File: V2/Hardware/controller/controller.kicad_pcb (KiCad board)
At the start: 2 copper layers, 50 parts, among them J0 Molex_PSU_F, J2 Flat_7seg_F, J3 Rpi_DATA_F_3.3V, Q0 BD139-16, Q1 BD139-16, Q2 BD139-16, Q3 BD139-16, Q4 BD139-16, Q5 BD139-16, Q6 BD139-16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

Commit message: Update files
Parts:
- C5: value 1000uF 35V LOW ESR -> 100uF 25V LOW ESR; footprint Capacitor_THT:CP_Radial_D13.0mm_P5.00mm -> Capacitor_THT:CP_Radial_D6.3mm_P2.50mm
- moved C5 4.00 mm to (138.0, 107.0)
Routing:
- net Earth: track 514.3 -> 563.1 mm
- net /+12V: track 239.9 -> 251.5 mm
- net /5V+: track 77.5 -> 87.2 mm
- net Net-(Q0-Pad3): track 4.03 -> 5.15 mm

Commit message: update capacitors
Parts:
- C5: value 100uF 25V LOW ESR -> 1000uF 35V LOW ESR; footprint Capacitor_THT:CP_Radial_D6.3mm_P2.50mm -> Capacitor_THT:CP_Radial_D12.5mm_P5.00mm
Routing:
- net Earth: track 563.1 -> 558.4 mm

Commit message: Update controller
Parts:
- added C6: 1nF, Capacitor_THT:C_Disc_D5.0mm_W2.5mm_P5.00mm, F.Cu at (145.0, 43.0)
- added L0: 22uH, Inductor_THT:L_Axial_L7.0mm_D3.3mm_P10.16mm_Horizontal_Fastron_MICC, F.Cu at (125.0, 65.0)
- C1: value 47uF -> 10uF 16V LOW ESR; footprint Capacitor_THT:CP_Radial_D10.0mm_P5.00mm -> Capacitor_THT:CP_Radial_D5.0mm_P2.00mm
- moved C3 19.2 mm to (131.0, 43.0)
- moved C2 10.8 mm to (138.0, 43.0)
- moved R7 10.4 mm to (121.0, 63.0), turned to 180 degrees
- moved C1 3.16 mm to (129.0, 51.0)
- moved D1 2.00 mm to (115.5, 57.0)
- moved R8 1.00 mm to (135.0, 46.0), turned to 0 degrees
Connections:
- C1 pad 1: /5V+ -> Net-(C1-Pad1)
- C2 pad 1: /5V+ -> Net-(C1-Pad1)
- C3 pad 1: /5V+ -> Net-(C1-Pad1)
- R7 pad 1: /5V+ -> Net-(D1-Pad2)
- R7 pad 2: Net-(D1-Pad2) -> /5V+
- R8 pad 2: /5V+ -> Net-(C1-Pad1)
- U1 pad 20: /5V+ -> Net-(C1-Pad1)
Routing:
- net Net-(C1-Pad1): track 0.00 -> 70.6 mm
- net /5V+: track 87.2 -> 51.7 mm
- net Earth: track 558.4 -> 591.2 mm
- net Net-(R8-Pad1): track 7.83 -> 14.4 mm
- net Net-(D1-Pad2): track 12.4 -> 11.4 mm

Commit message: revision 2 boards
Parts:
- added Screw: MountingHole_3.2mm_M3, MountingHole:MountingHole_3.2mm_M3, F.Cu at (109.0, 106.0)
- added Screw: MountingHole_3.2mm_M3, MountingHole:MountingHole_3.2mm_M3, F.Cu at (192.0, 104.0)
- added Screw: MountingHole_3.2mm_M3, MountingHole:MountingHole_3.2mm_M3, F.Cu at (204.0, 41.0)
- added Screw: MountingHole_3.2mm_M3, MountingHole:MountingHole_3.2mm_M3, F.Cu at (108.0, 68.0)
- J0: value Molex_PSU_F -> Molex_PSU; footprint PSU:conn_hdd_15-24-4441 -> KicadLib:conn_hdd_15-24-4449
- J2: value Flat_7seg_F -> 7SEG_12V; footprint Connector_PinHeader_2.54mm:PinHeader_2x05_P2.54mm_Horizontal -> Connector_IDC:IDC-Header_2x05-1MP_P2.54mm_Latch_Vertical
- J3: value Rpi_DATA_F_3.3V -> RPI_DATA_3.3V; footprint Connector_PinHeader_2.54mm:PinHeader_2x03_P2.54mm_Horizontal -> Connector_IDC:IDC-Header_2x05-1MP_P2.54mm_Latch_Vertical
- moved L0 35.4 mm to (94.0, 48.0), turned to 270 degrees
- moved R7 22.6 mm to (99.0, 58.0), turned to 90 degrees
- moved J3 12.1 mm to (98.0, 87.0)
- moved J0 11.2 mm to (99.0, 43.0), turned to 180 degrees
- moved R12 10.0 mm to (127.0, 91.0), turned to 90 degrees
- moved D1 8.43 mm to (109.5, 51.0), turned to 270 degrees
- moved J2 7.27 mm to (173.0, 104.0), turned to 270 degrees
- moved R11 5.10 mm to (120.0, 91.0), turned to 90 degrees
- moved R10 4.84 mm to (113.0, 91.0)
- moved R9 4.47 mm to (106.0, 90.2)
- moved R13 3.01 mm to (123.0, 39.0)
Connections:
- J3 pad 1: /BIT_D -> /BIT_A
- J3 pad 2: Net-(J3-Pad2) -> Earth
- J3 pad 3: /BIT_C -> /BIT_B
- J3 pad 4: /BIT_C -> Earth
- J3 pad 5: /BIT_B -> /BIT_C
- J3 pad 6: /BIT_A -> Earth
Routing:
- net /SEG_C: track 17.8 -> 67.3 mm
- net /SEG_B: track 25.6 -> 71.2 mm
- net /SEG_A: track 36.9 -> 79.6 mm
- net /BIT_B: track 83.2 -> 41.9 mm, vias 2 -> 0
- net Net-(C1-Pad1): track 70.6 -> 105.2 mm
- net /5V+: track 51.7 -> 20.2 mm
- net /SEG_G: track 58.7 -> 37.8 mm
- net Net-(D5-Pad2): track 26.7 -> 8.00 mm
- net /SEG_F: track 47.1 -> 29.7 mm
- net /BIT_A: track 58.6 -> 44.0 mm
- net /SEG_E: track 34.3 -> 21.9 mm
- net Earth: track 591.2 -> 601.1 mm
- net /BIT_D: track 38.7 -> 45.1 mm
- net Net-(D6-Pad2): track 19.1 -> 25.1 mm
- net Net-(D3-Pad2): track 14.0 -> 8.00 mm
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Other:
- board text added: "125 mm"
- board text added: "83 mm"
- board text removed: "12.5cm"
- board text removed: "8cm"

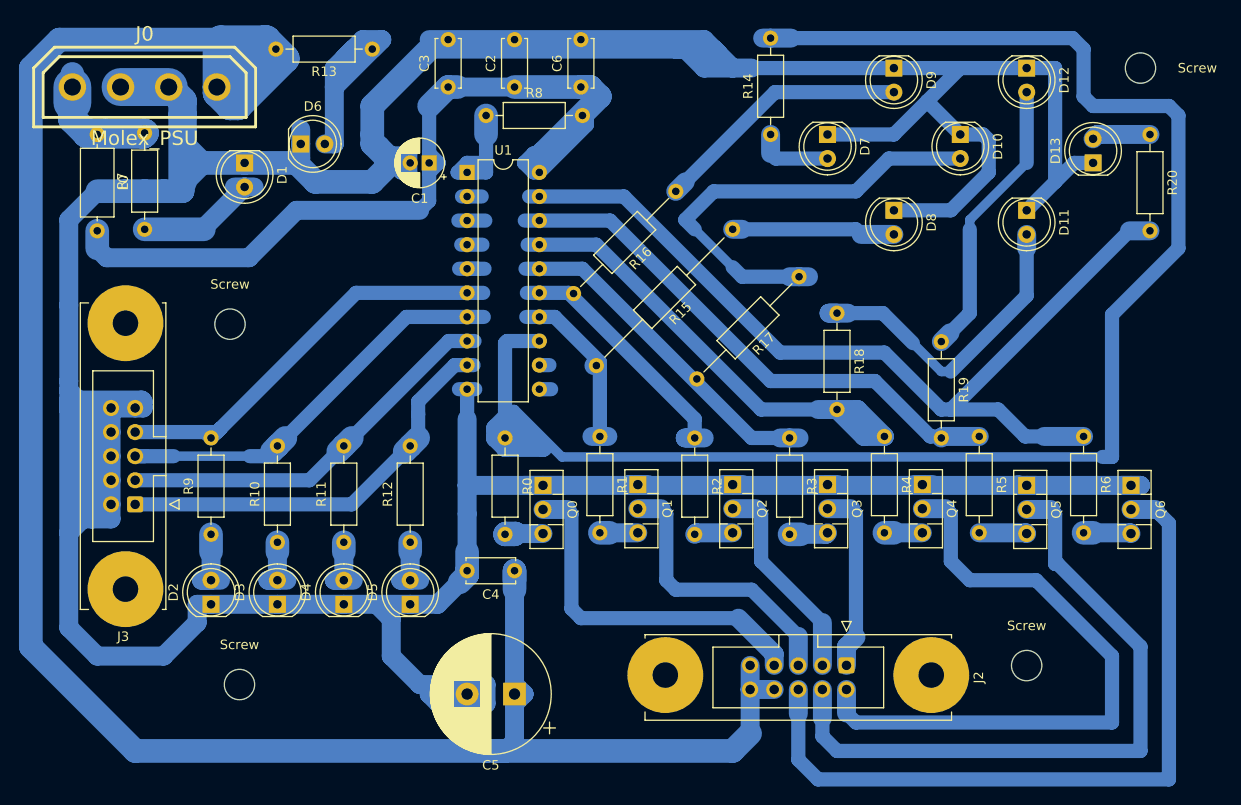
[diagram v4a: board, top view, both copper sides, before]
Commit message: Remove version 1 board
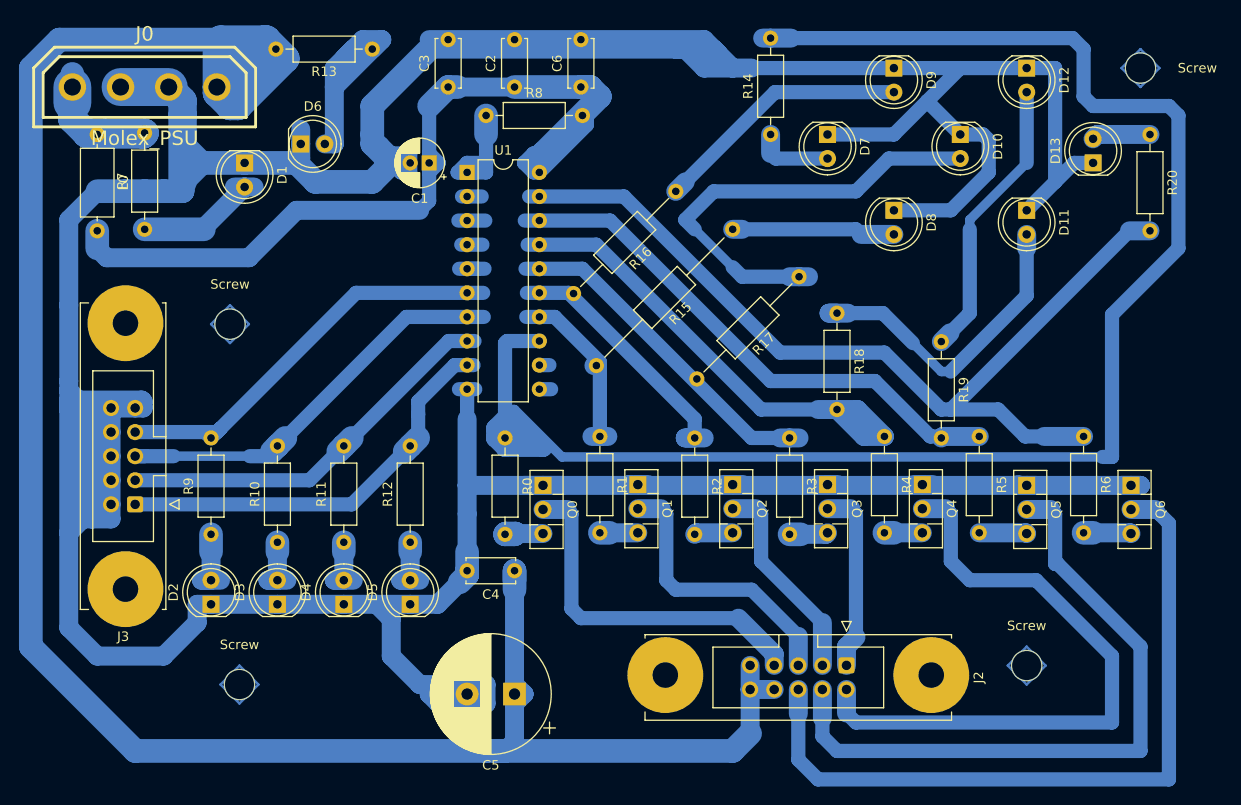
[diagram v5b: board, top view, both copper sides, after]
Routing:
- net (no net): track 0.00 -> 45.3 mm, vias 0 -> 4
